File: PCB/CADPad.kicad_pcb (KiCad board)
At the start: 2 copper layers, 175.4 x 142.7 mm, 108 parts, among them CN1 S2B-PH-SM4-TB, Q1 FS8205A_C2830320, SW1 EC11E15244G1, SW2 EC11E15244G1, U1 Nice_Nano_V2, U2 SL2.1S, U3 DW01A_C351410, U4 MCP73831T-2ACI/OT

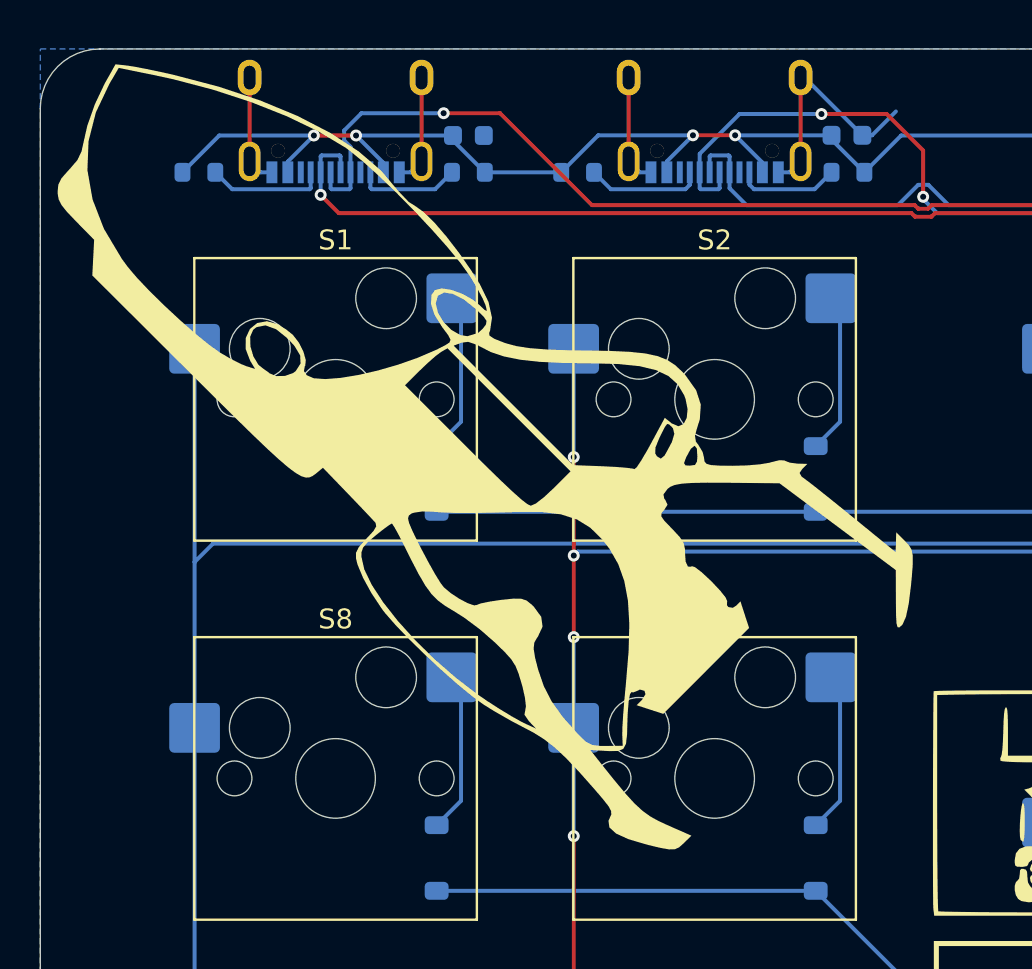
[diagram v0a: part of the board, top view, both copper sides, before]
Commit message: assigning LSCS numbers and regenerating PCB-CAD
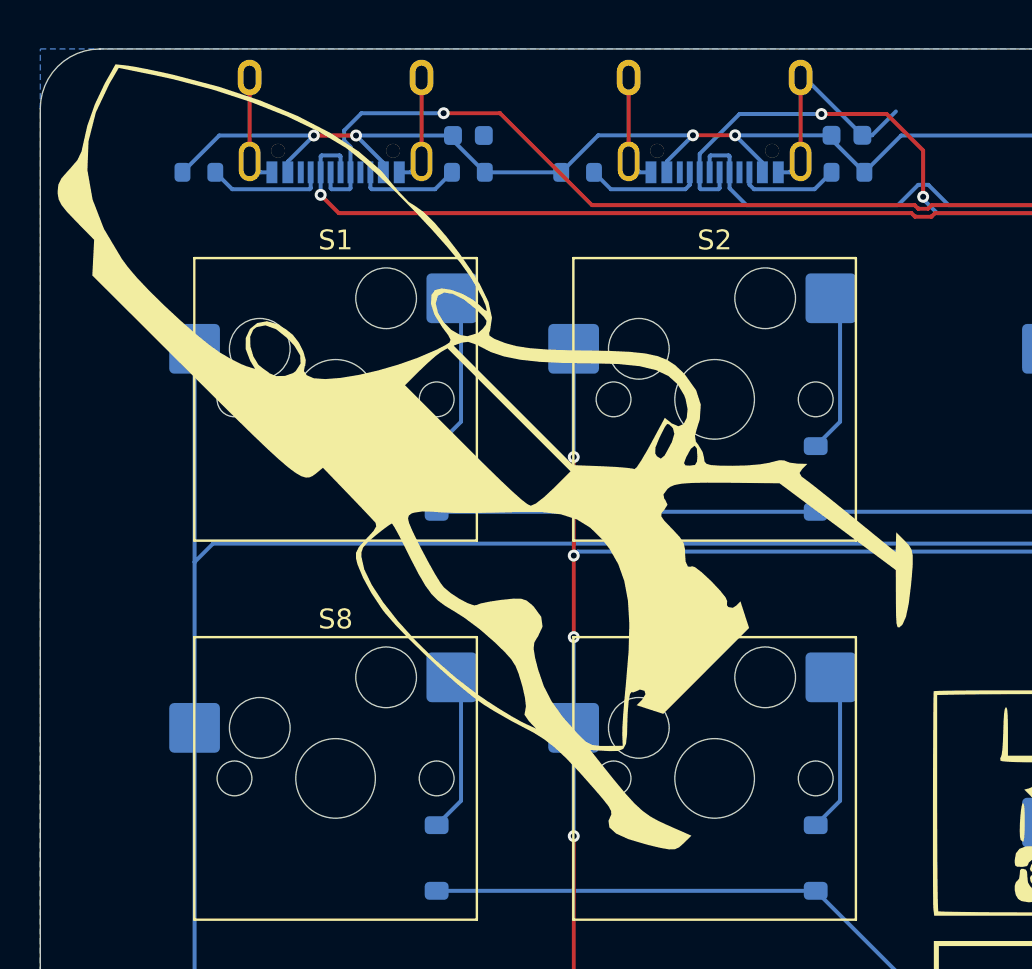
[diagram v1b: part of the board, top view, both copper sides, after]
